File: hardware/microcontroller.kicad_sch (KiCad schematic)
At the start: 20 parts, among them J5 1x2 jumper right-angle, J6 Conn_02x03_Odd_Even, J7 1x2 jumper right-angle, U1 74LVC2G125, U15 74LVC138A, U17 74LVC138A

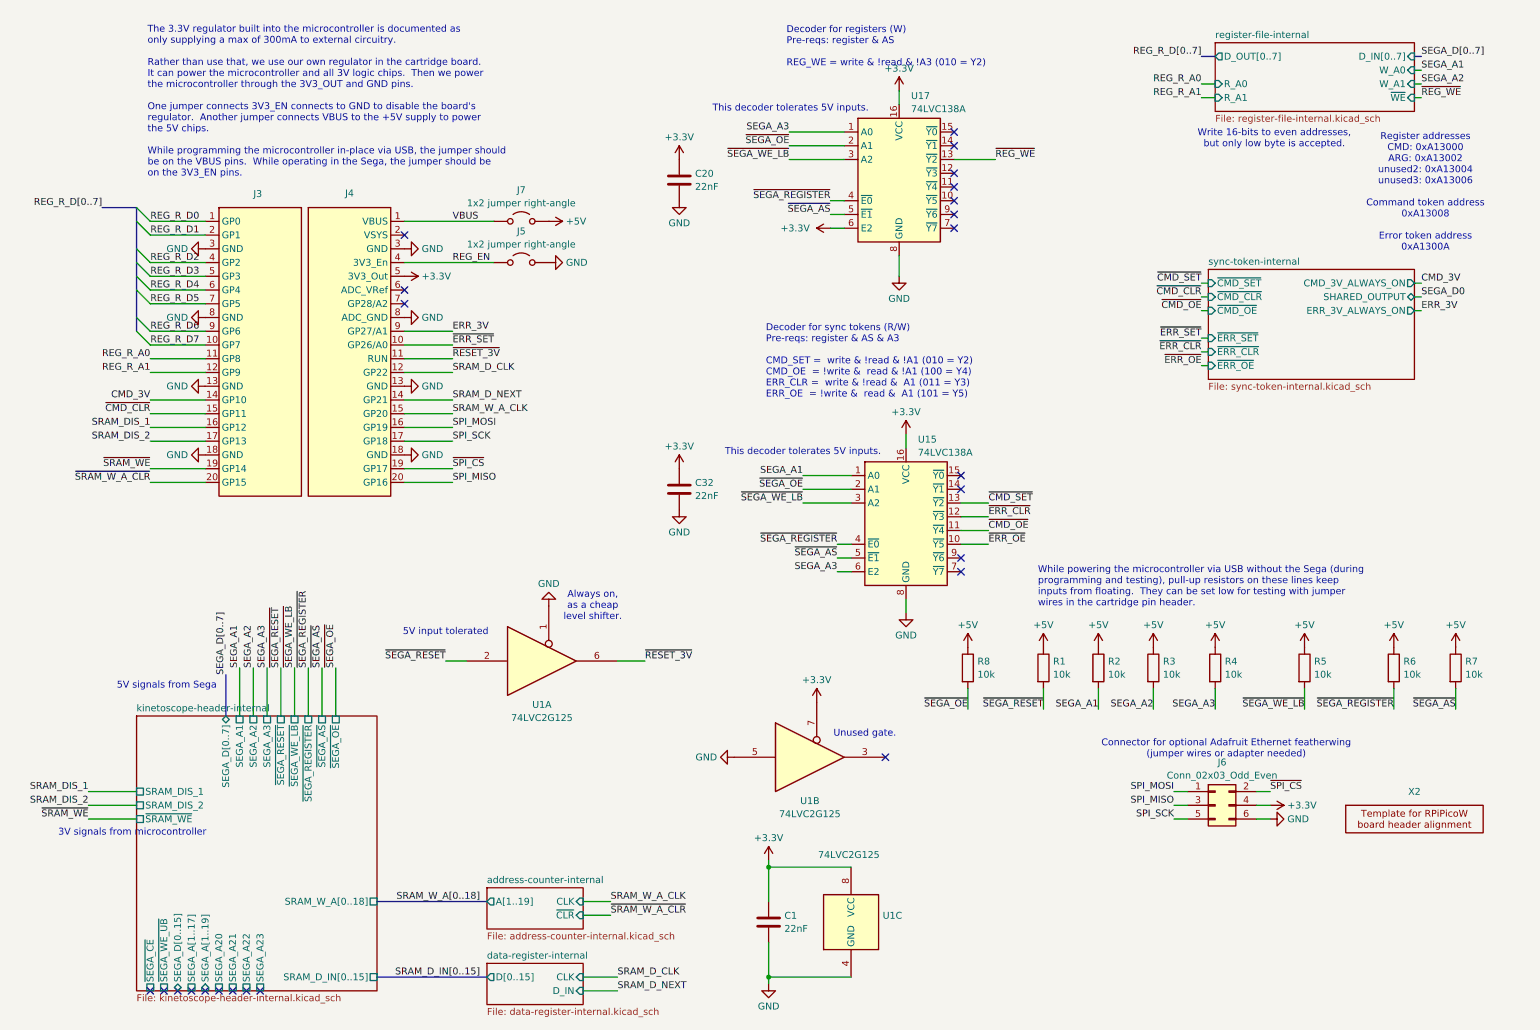
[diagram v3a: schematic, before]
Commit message: Improve uC board assembly further
Change the register file CD74HC670M96 with SN74AHC373PWR and an
inverter, which is more easily available from JLCPCB.

This is not an exact replacement, as we replaced 2x 4x4 register files
with 2x 8-bit latches.  So instead of 4x 8-bit registers, we now only
have 2x 8-bit registers, but we only used 2 to begin with.

The new register hardware required us to change the address decoding
and the actual addresses of the registers.  Instead of 0xA13000 and
0xA13002, we now write to 0xA13010 and 0xA13012.
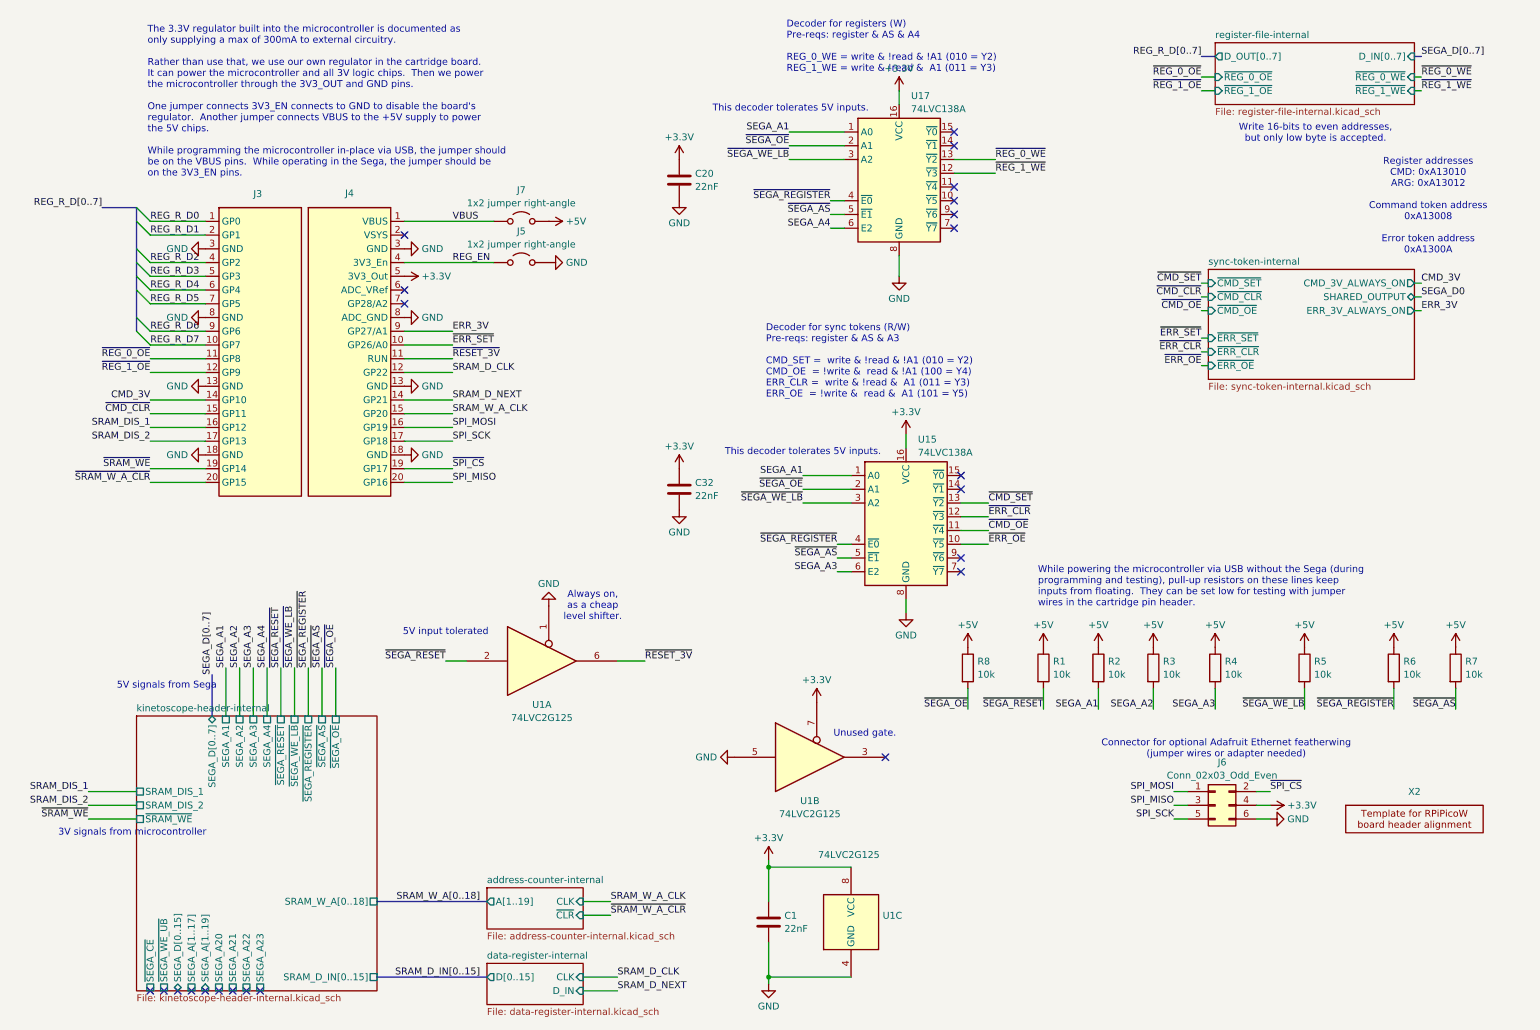
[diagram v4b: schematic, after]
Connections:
- net +3.3V: no longer U17.6 (E2)
- net SEGA_A1: now also U17.1 (A0)
- net SEGA_A3: no longer U17.1 (A0)
- net ~{REG_1_WE}: now reaches U17.12 (~{Y3})
- net REG_R_A0 renamed ~{REG_0_OE}
- net REG_R_A1 renamed ~{REG_1_OE}
- net ~{REG_WE} renamed ~{REG_0_WE}
- new net SEGA_A4: U17.6 (E2)
- no-connect marks 24 -> 23
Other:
- sheet kinetoscope-header-internal ports: added SEGA_A4; removed none
- sheet register-file-internal ports: added ~{REG_0_OE}, ~{REG_0_WE}, ~{REG_1_OE}, ~{REG_1_WE}; removed R_A0, R_A1, W_A0, W_A1, ~{WE}
- note added: "Decoder for registers (W) Pre-reqs: register & AS & A4 REG_0_WE = write & !read & !A1 (010 = Y2) REG_1_WE = write & !read & A1 (011 = Y3)"
- note added: "Register addresses CMD: 0xA13010 ARG: 0xA13012 Command token address 0xA13008 Error token address 0xA1300A"
- note removed: "Decoder for registers (W) Pre-reqs: register & AS REG_WE = write & !read & !A3 (010 = Y2)"
- note removed: "Register addresses CMD: 0xA13000 ARG: 0xA13002 unused2: 0xA13004 unused3: 0xA13006 Command token address 0xA13008 Error token address 0xA1300A"

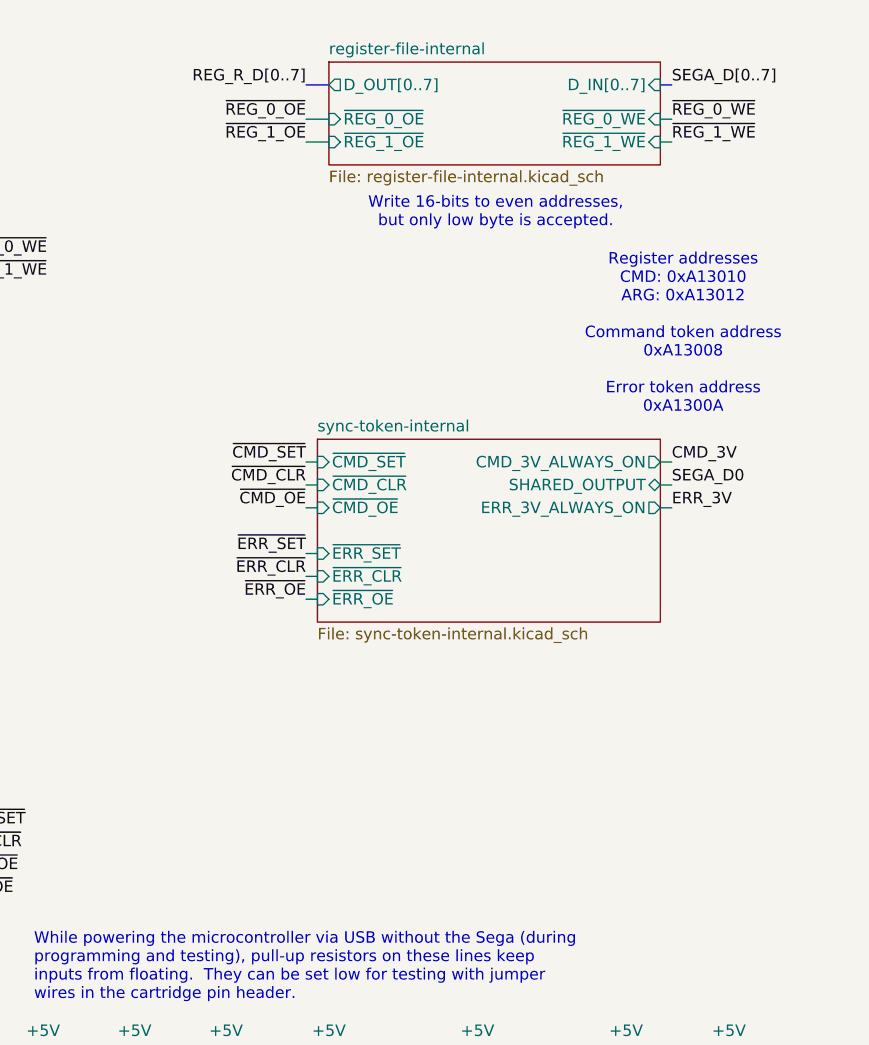
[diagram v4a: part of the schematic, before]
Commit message: Add test pads to uC board
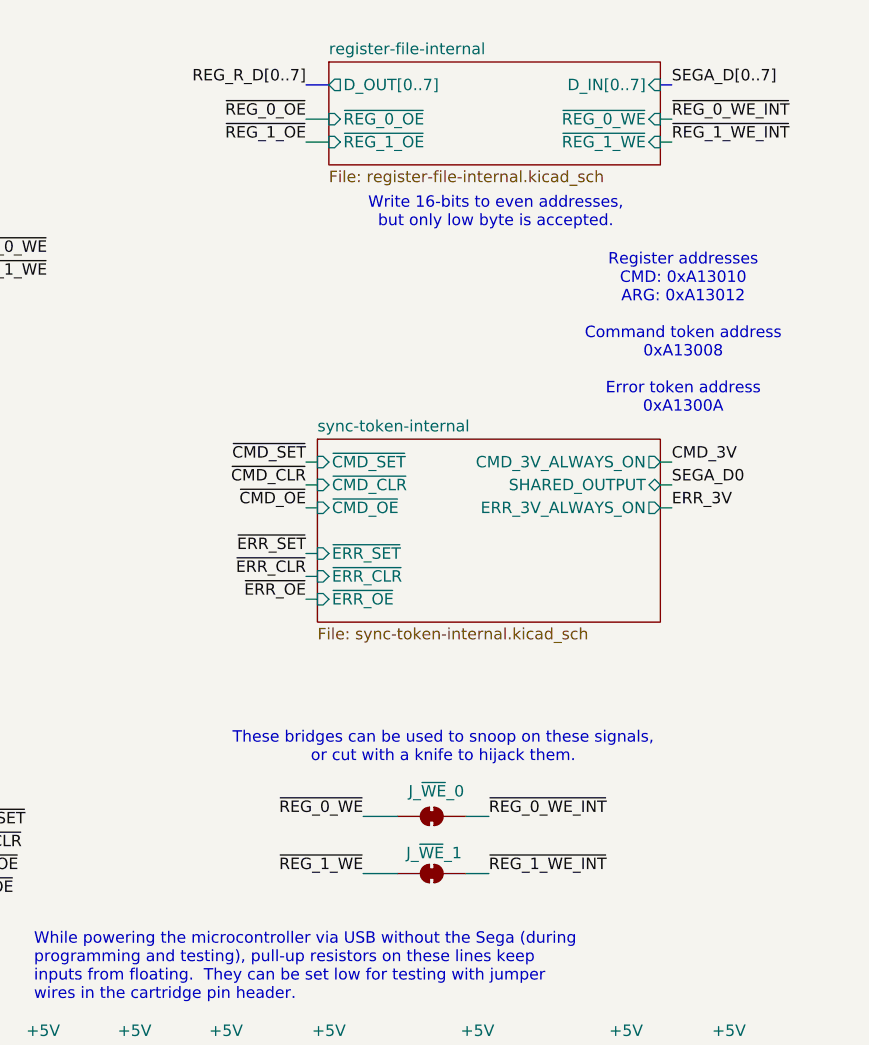
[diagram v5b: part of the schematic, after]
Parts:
- added J_~{WE}_0, J_~{WE}_1: ~, Jumper:SolderJumper-2_P1.3mm_Bridged_RoundedPad1.0x1.5mm, symbol Jumper:SolderJumper_2_Bridged
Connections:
- net ~{REG_0_WE}: now also J_~{WE}_0.1 (A)
- net ~{REG_1_WE}: now also J_~{WE}_1.1 (A)
- new net ~{REG_0_WE_INT}: J_~{WE}_0.2 (B)
- new net ~{REG_1_WE_INT}: J_~{WE}_1.2 (B)
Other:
- note added: "These bridges can be used to snoop on these signals, or cut with a knife to hijack them."
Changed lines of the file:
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@@
 	(wire
 		(pts
+			(xy 236.22 101.6) (xy 240.03 101.6)
+		)
+		(stroke
+			(width 0)
+			(type default)
+		)
+	)
+	(wire
+		(pts
 			(xy 82.55 76.2) (xy 91.44 76.2)
 		)
@@
 	(wire
 		(pts
+			(xy 247.65 107.95) (xy 250.19 107.95)
+		)
+		(stroke
+			(width 0)
+			(type default)
+		)
+	)
+	(wire
+		(pts
 			(xy 35.56 86.36) (xy 45.72 86.36)
 		)
@@
 	(wire
 		(pts
+			(xy 247.65 101.6) (xy 250.19 101.6)
+		)
+		(stroke
+			(width 0)
+			(type default)
+		)
+	)
+	(wire
+		(pts
 			(xy 35.56 96.52) (xy 45.72 96.52)
 		)
@@
 		)
 	)
+	(wire
+		(pts
+			(xy 236.22 107.95) (xy 240.03 107.95)
+		)
+		(stroke
+			(width 0)
+			(type default)
+		)
+	)
 	(bus
 		(pts
@@
 		)
 	)
+	(text "These bridges can be used to snoop on these signals,\nor cut with a knife to hijack them."
+		(exclude_from_sim no)
+		(at 245.11 93.98 0)
+		(effects
+			(font
+				(size 1.27 1.27)
+			)
+		)
+	)
 	(text "3V signals from microcontroller"
 		(exclude_from_sim no)
@@
 		)
 	)
+	(label "~{REG_0_WE_INT}"
+		(at 250.19 101.6 0)
+		(fields_autoplaced yes)
+		(effects
+			(font
+				(size 1.27 1.27)
+			)
+			(justify left bottom)
+		)
+	)
 	(label "REG_R_D6"
 		(at 35.56 71.12 0)
@@
 		)
 	)
+	(label "~{REG_1_WE_INT}"
+		(at 250.19 107.95 0)
+		(fields_autoplaced yes)
+		(effects
+			(font
+				(size 1.27 1.27)
+			)
+			(justify left bottom)
+		)
+	)
 	(label "SEGA_A3"
 		(at 162.56 115.57 180)
@@
 		)
 	)
+	(label "~{REG_1_WE}"
+		(at 236.22 107.95 180)
+		(fields_autoplaced yes)
+		(effects
+			(font
+				(size 1.27 1.27)
+			)
+			(justify right bottom)
+		)
+	)
 	(label "~{SPI_CS}"
 		(at 91.44 96.52 0)
@@
 		)
 	)
-	(label "~{REG_1_WE}"
+	(label "~{REG_1_WE_INT}"
 		(at 270.51 26.67 0)
 		(fields_autoplaced yes)
@@
 		)
 	)
-	(label "~{REG_0_WE}"
+	(label "~{REG_0_WE_INT}"
 		(at 270.51 24.13 0)
 		(fields_autoplaced yes)
@@
 		)
 	)
+	(label "~{REG_0_WE}"
+		(at 236.22 101.6 180)
+		(fields_autoplaced yes)
+		(effects
+			(font
+				(size 1.27 1.27)
+			)
+			(justify right bottom)
+		)
+	)
 	(label "CMD_3V"
 		(at 35.56 83.82 180)
@@
 	)
 	(symbol
+		(lib_id "Jumper:SolderJumper_2_Bridged")
+		(at 243.84 101.6 0)
+		(unit 1)
+		(exclude_from_sim yes)
+		(in_bom no)
+		(on_board yes)
+		(dnp no)
+		(property "Reference" "J_~{WE}_0"
+			(at 244.348 98.806 0)
+			(effects
+				(font
+					(size 1.27 1.27)
+				)
+			)
+		)
+		(property "Value" "~"
+			(at 243.84 99.7339 0)
+			(effects
+				(font
+					(size 1.27 1.27)
+				)
+			)
+		)
+		(property "Footprint" "Jumper:SolderJumper-2_P1.3mm_Bridged_RoundedPad1.0x1.5mm"
+			(at 243.84 101.6 0)
+			(effects
+				(font
+					(size 1.27 1.27)
+				)
+				(hide yes)
+			)
+		)
+		(property "Datasheet" "~"
+			(at 243.84 101.6 0)
+			(effects
+				(font
+					(size 1.27 1.27)
+				)
+				(hide yes)
+			)
+		)
+		(property "Description" "Solder Jumper, 2-pole, closed/bridged"
+			(at 243.84 101.6 0)
+			(effects
+				(font
+					(size 1.27 1.27)
+				)
+				(hide yes)
+			)
+		)
+		(pin "1"
+		)
+		(pin "2"
+		)
+		(instances
+			(project "microcontroller"
+				(path "/eb0e957f-b2ea-4261-97c1-e28148a3f6e1"
+					(reference "J_~{WE}_0")
+					(unit 1)
+				)
+			)
+		)
+	)
+	(symbol
 		(lib_id "power:+5V")
 		(at 248.92 129.54 0)
@@
 					(unit 1)
 				)
+			)
+		)
+	)
+	(symbol
+		(lib_id "Jumper:SolderJumper_2_Bridged")
+		(at 243.84 107.95 0)
+		(unit 1)
+		(exclude_from_sim yes)
+		(in_bom no)
+		(on_board yes)
+		(dnp no)
+		(property "Reference" "J_~{WE}_1"
+			(at 244.094 105.664 0)
+			(effects
+				(font
+					(size 1.27 1.27)
+				)
+			)
+		)
+		(property "Value" "~"
+			(at 243.84 106.0839 0)
+			(effects
+				(font
+					(size 1.27 1.27)
+				)
+			)
+		)
+		(property "Footprint" "Jumper:SolderJumper-2_P1.3mm_Bridged_RoundedPad1.0x1.5mm"
+			(at 243.84 107.95 0)
+			(effects
+				(font
+					(size 1.27 1.27)
+				)
+				(hide yes)
+			)
+		)
+		(property "Datasheet" "~"
+			(at 243.84 107.95 0)
+			(effects
+				(font
+					(size 1.27 1.27)
+				)
+				(hide yes)
+			)
+		)
+		(property "Description" "Solder Jumper, 2-pole, closed/bridged"
+			(at 243.84 107.95 0)
+			(effects
+				(font
+					(size 1.27 1.27)
+				)
+				(hide yes)
+			)
+		)
+		(pin "1"
+		)
+		(pin "2"
+		)
+		(instances
+			(project "microcontroller"
+				(path "/eb0e957f-b2ea-4261-97c1-e28148a3f6e1"
+					(reference "J_~{WE}_1")
+					(unit 1)
+				)

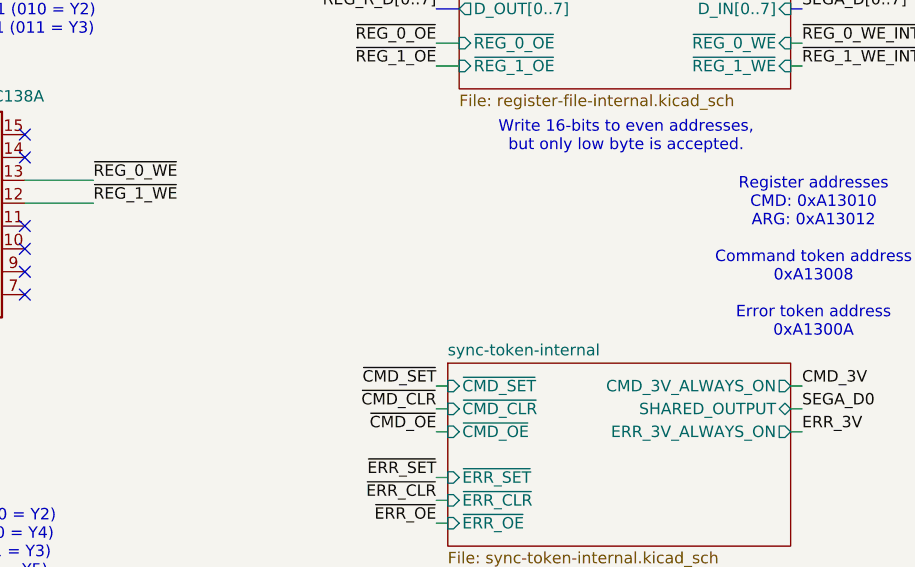
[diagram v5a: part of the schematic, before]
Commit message: Add note about possible address conflict
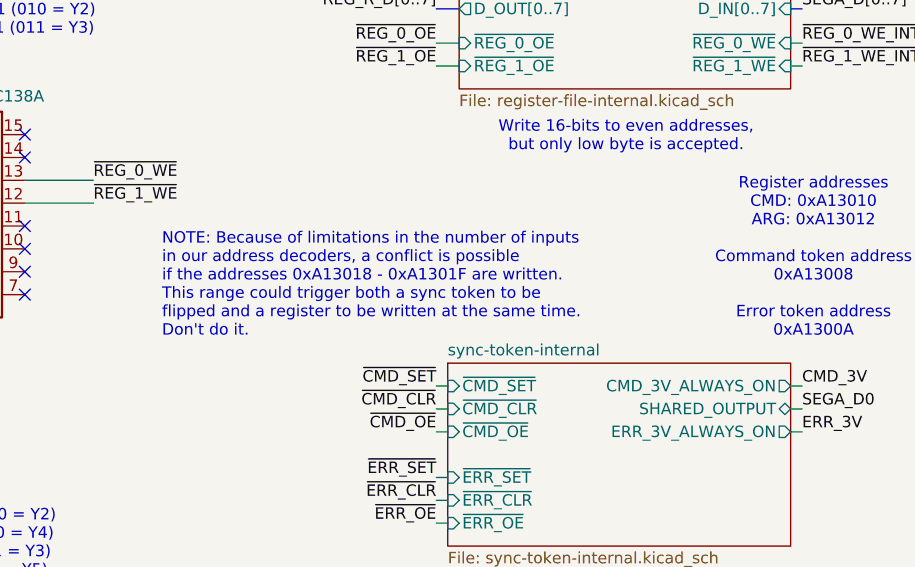
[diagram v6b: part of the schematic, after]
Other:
- note added: "NOTE: Because of limitations in the number of inputs in our address decoders, a conflict is possible if the addresses 0xA13018 - 0xA1301F are written. This range could trigger both a sync token to be flipped and a register to be written at the same time. Don't do it."
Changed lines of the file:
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@@
+		)
+	)
+	(text "NOTE: Because of limitations in the number of inputs\nin our address decoders, a conflict is possible\nif the addresses 0xA13018 - 0xA1301F are written.\nThis range could trigger both a sync token to be\nflipped and a register to be written at the same time.\nDon't do it."
+		(exclude_from_sim no)
+		(at 199.39 45.212 0)
+		(effects
+			(font
+				(size 1.27 1.27)
+			)
+			(justify left top)
 		)
 	)

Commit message: Add part numbers for all headers
You can still choose to leave these off of an assembly order and populate them yourself.
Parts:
- J5, J7: JLCPCB Part Number (none) -> C6952593
- J6: JLCPCB Part Number (none) -> C6825448; Mouser Part Number (none) -> 200-SSW10301TD; Part Number (none) -> SSW-103-01-T-D
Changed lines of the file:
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@@
 			)
 		)
-		(property "JLCPCB Part Number" ""
+		(property "JLCPCB Part Number" "C6952593"
 			(at 104.14 58.42 0)
 			(effects
@@
 			)
 		)
+		(property "JLCPCB Part Number" "C6825448"
+			(at 232.41 158.75 0)
+			(effects
+				(font
+					(size 1.27 1.27)
+				)
+				(hide yes)
+			)
+		)
+		(property "Mouser Part Number" "200-SSW10301TD"
+			(at 232.41 158.75 0)
+			(effects
+				(font
+					(size 1.27 1.27)
+				)
+				(hide yes)
+			)
+		)
+		(property "Part Number" "SSW-103-01-T-D"
+			(at 232.41 158.75 0)
+			(effects
+				(font
+					(size 1.27 1.27)
+				)
+				(hide yes)
+			)
+		)
 		(pin "1"
 		)
@@
 			)
 		)
-		(property "JLCPCB Part Number" ""
+		(property "JLCPCB Part Number" "C6952593"
 			(at 104.14 50.8 0)
 			(effects
